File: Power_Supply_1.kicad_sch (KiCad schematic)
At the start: 8 parts

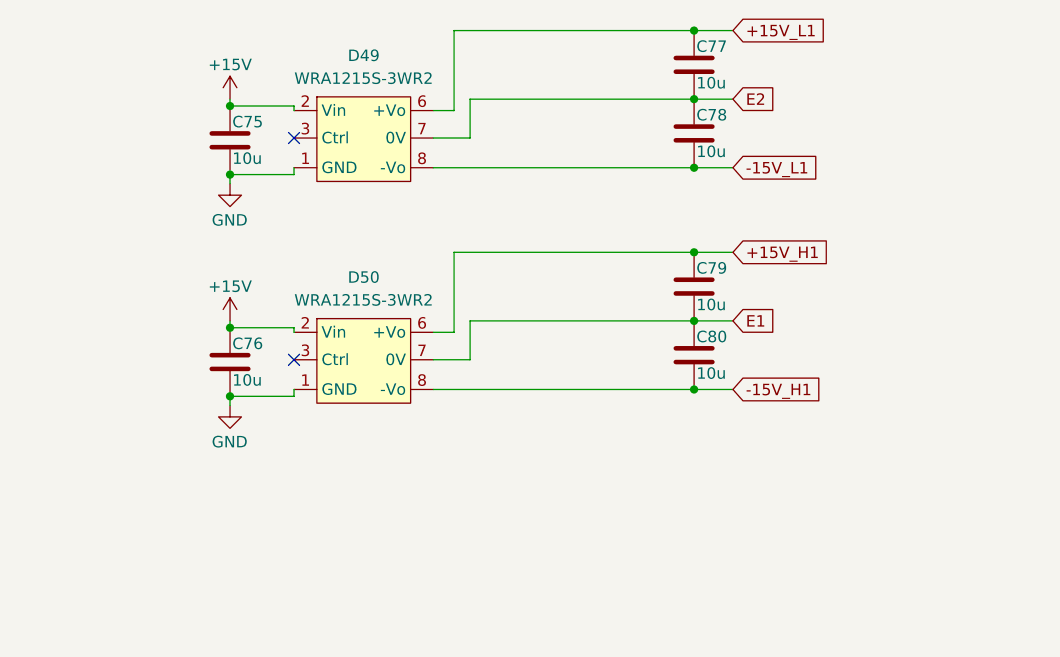
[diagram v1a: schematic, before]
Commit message: Изменил схему
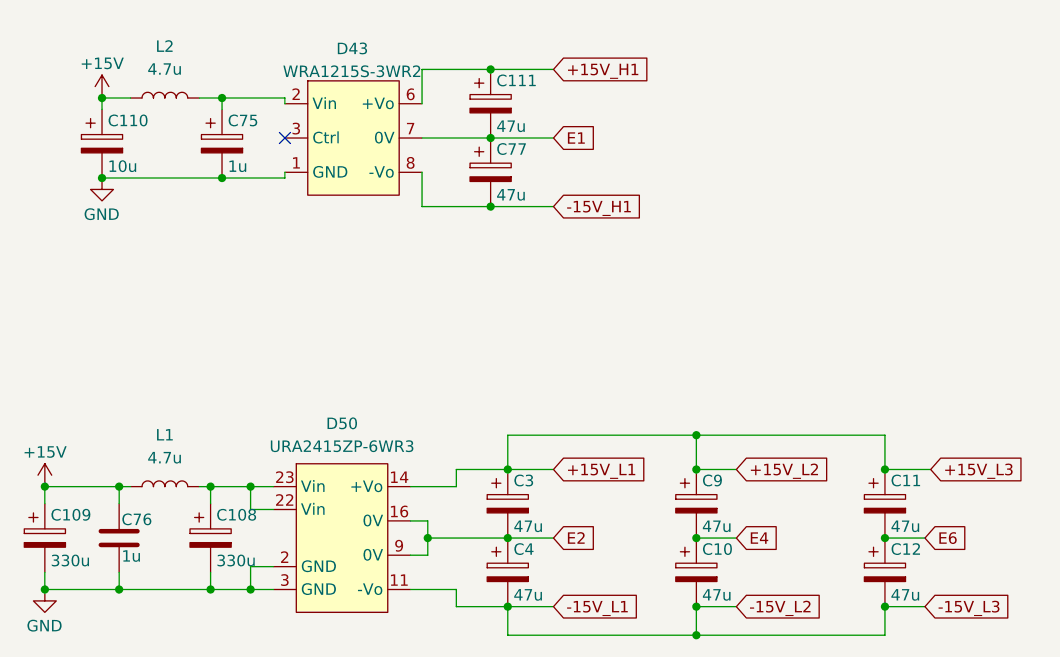
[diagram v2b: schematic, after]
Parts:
- removed C75, C77, C78, C79, C80: 10u, Capacitor_SMD:C_1210_3225Metric_Pad1.33x2.70mm_HandSolder, symbol Device:C
- removed D49: WRA1215S-3WR2, Mornsun:WRA1215S-3WR2, symbol Morsun:WRA1215S-3WR2
- added C10, C11, C111, C12, C3, C4, C77, C9: 47u, Capacitor_Tantalum_SMD:CP_EIA-7343-31_Kemet-D, symbol Device:C_Polarized
- added C108, C109: 330u, symbol Device:C_Polarized
- added C110: 10u, Capacitor_Tantalum_SMD:CP_EIA-7343-31_Kemet-D, symbol Device:C_Polarized
- added C75: 1u, Capacitor_Tantalum_SMD:CP_EIA-3528-21_Kemet-B, symbol Device:C_Polarized
- added D43: WRA1215S-3WR2, Mornsun:WRA_S-3WR2, symbol Morsun:WRA1215S-3WR2
- added L1, L2: 4.7u, Inductor_SMD:L_1812_4532Metric_Pad1.30x3.40mm_HandSolder, symbol Device:L
- C76: value 10u -> 1u
- D50: value WRA1215S-3WR2 -> URA2415ZP-6WR3; footprint Mornsun:WRA1215S-3WR2 -> Mornsun:URA_ZP-6WR3
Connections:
- net +15V: now also C109.1, C110.1, L1.1, L2.1; no longer D50.2 (Vin)
- net +15V_H1: now also C111.1, D43.6 (+Vo); no longer D50.6 (+Vo)
- net +15V_L1: now also D50.14 (+Vo), C11.1, C3.1, C9.1
- net -15V_H1: now also C77.2, D43.8 (-Vo); no longer D50.8 (-Vo)
- net -15V_L1: now also D50.11 (-Vo), C10.2, C12.2, C4.2
- net E1: now also C111.2, C77.1, D43.7 (0V); no longer D50.7 (0V)
- net E2: now also D50.16 (0V), D50.9 (0V), C3.2, C4.1
- net GND: now also D50.2 (GND), D50.3 (GND), C108.2, C109.2, C110.2, C75.2, D43.1 (GND); no longer D50.1 (GND)
- new net: C75.1, D43.2 (Vin), L2.2
- new net: C108.1, D50.22 (Vin), D50.23 (Vin), L1.2
- new net E4: C10.1, C9.2
- new net E6: C11.2, C12.1
- no-connect marks 2 -> 1
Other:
- moved on the sheet: C76

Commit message: Разместил все три стойки в своей области
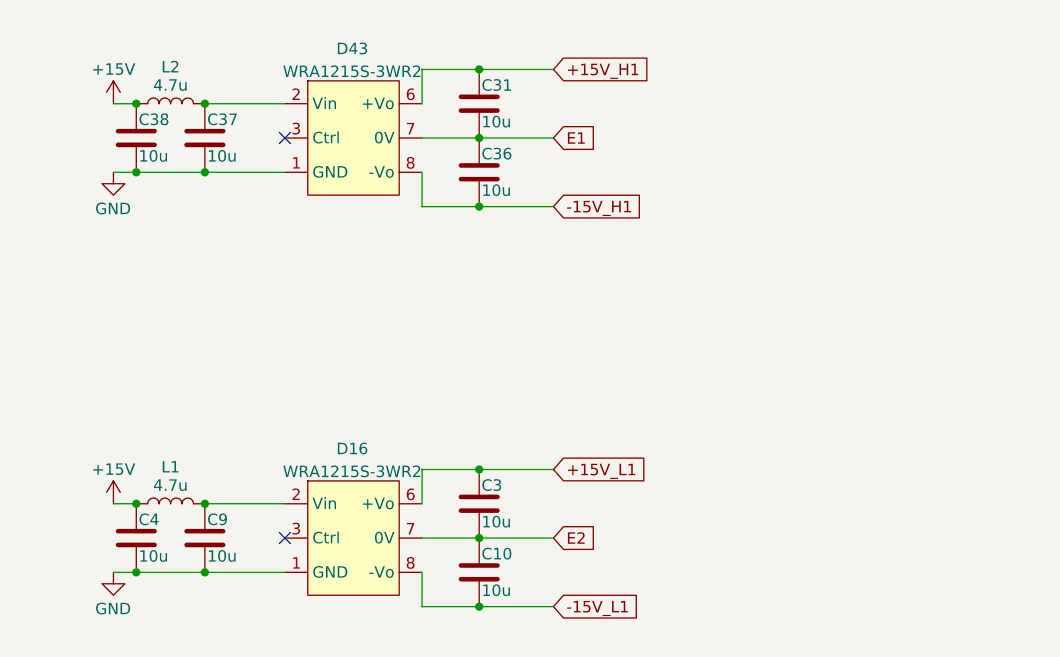
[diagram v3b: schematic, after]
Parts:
- removed C10, C11, C111, C12, C3, C4, C77, C9: 47u, Capacitor_Tantalum_SMD:CP_EIA-7343-31_Kemet-D, symbol Device:C_Polarized
- removed C108, C109: 330u, symbol Device:C_Polarized
- removed C110: 10u, Capacitor_Tantalum_SMD:CP_EIA-7343-31_Kemet-D, symbol Device:C_Polarized
- removed C75: 1u, Capacitor_Tantalum_SMD:CP_EIA-3528-21_Kemet-B, symbol Device:C_Polarized
- removed C76: 1u, Capacitor_SMD:C_1210_3225Metric_Pad1.33x2.70mm_HandSolder, symbol Device:C
- removed D50: URA2415ZP-6WR3, Mornsun:URA_ZP-6WR3, symbol Morsun:WRA1215S-3WR2
- added C10, C3, C31, C36, C37, C38, C4, C9: 10u, Capacitor_SMD:C_1210_3225Metric_Pad1.33x2.70mm_HandSolder, symbol Device:C
- added D16: WRA1215S-3WR2, Mornsun:WRA_S-3WR2, symbol Morsun:WRA1215S-3WR2
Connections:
- net +15V: now also C38.1, C4.1
- net +15V_H1: now also C31.1
- net +15V_L1: now also C3.1, D16.6 (+Vo)
- net -15V_H1: now also C36.2
- net -15V_L1: now also C10.2, D16.8 (-Vo)
- net E1: now also C31.2, C36.1
- net E2: now also C10.1, C3.2, D16.7 (0V)
- net GND: now also C37.2, C38.2, C4.2, C9.2, D16.1 (GND)
- net at D43.2 (Vin), L2.2: now also C37.1
- net at L1.2: now also C9.1, D16.2 (Vin)
- no-connect marks 1 -> 2
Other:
- moved on the sheet: L2

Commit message: VER2.1: добавил схему в доки
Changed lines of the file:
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@@
 (kicad_sch
-	(version 20231120)
+	(version 20250114)
 	(generator "eeschema")
-	(generator_version "8.0")
+	(generator_version "9.0")
 	(paper "A4")
 	(junction
